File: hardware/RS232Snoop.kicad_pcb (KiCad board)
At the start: 2 copper layers, 29 x 13.2 mm, 11 parts, among them J3 Conn_01x02, J4 Screw_Terminal_01x03, J5 Screw_Terminal_01x03

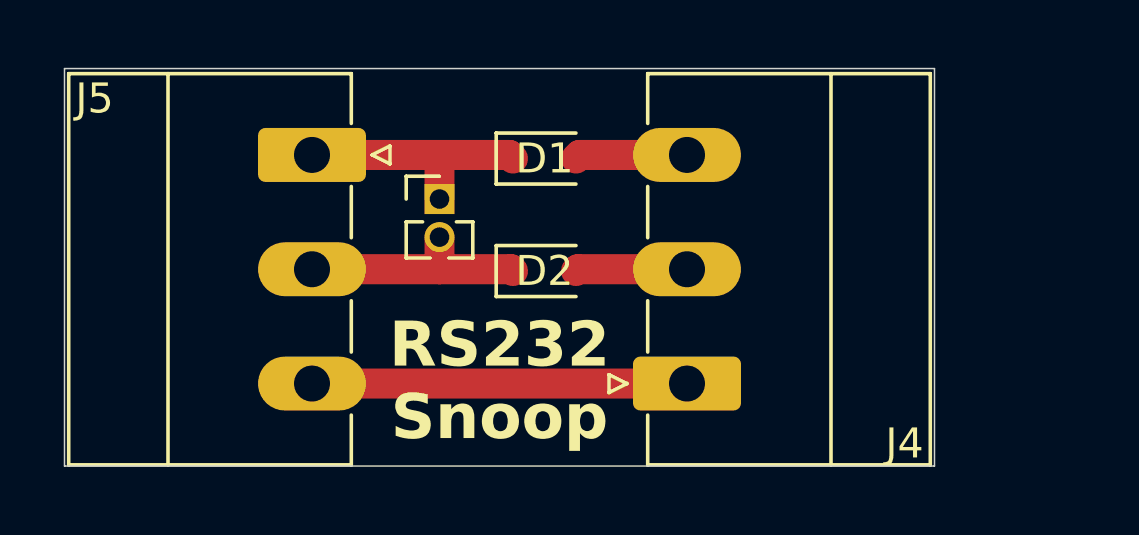
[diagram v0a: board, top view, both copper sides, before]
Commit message: Added headers for straight or crossover
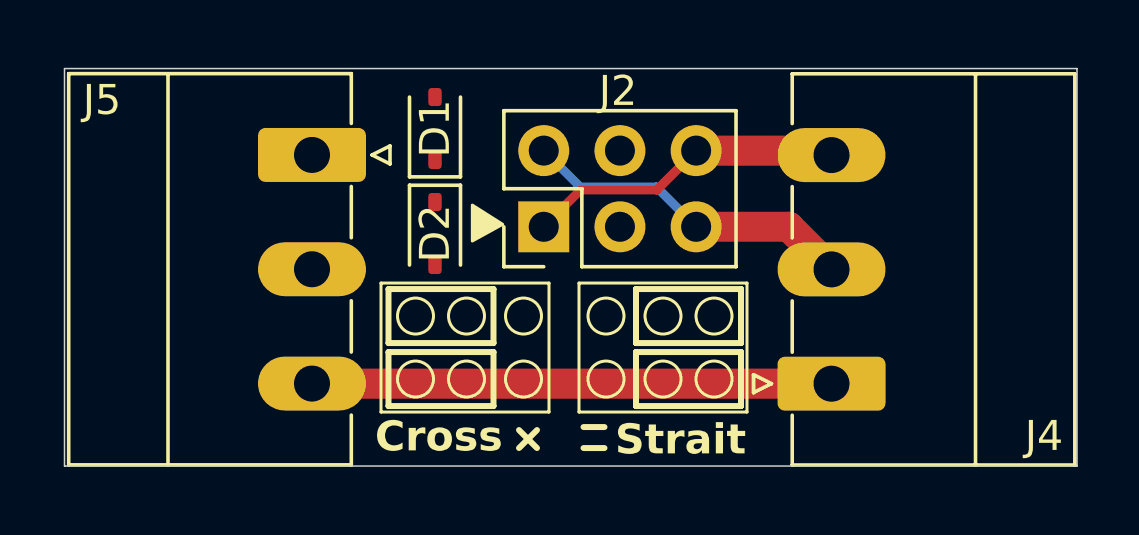
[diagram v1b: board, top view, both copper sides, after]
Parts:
- removed J3: Conn_01x02, Connector_PinHeader_1.27mm:PinHeader_1x02_P1.27mm_Vertical
- added J2: Conn_02x03_Odd_Even, Connector_PinHeader_2.54mm:PinHeader_2x03_P2.54mm_Vertical, F.Cu at (114.7, 56.0)
- moved ? 5.10 mm to (132.4, 50.9)
- moved J4 4.82 mm to (124.3, 61.3)
- moved D2 3.86 mm to (111.1, 56.2), turned to -90 degrees
- moved D1 3.78 mm to (111.1, 52.8), turned to 90 degrees
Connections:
- net Net-(J4-Pin_1) renamed SGND
- D1 pad 2: Net-(D1-A) -> B_TX
- D2 pad 2: Net-(D2-A) -> B_RX
- J4 pad 2: Net-(D2-A) -> A_RX
- J4 pad 3: Net-(D1-A) -> A_TX
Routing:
- net A_RX: track 0.00 -> 11.2 mm
- net A_TX: track 0.00 -> 10.7 mm
- net Net-(D1-K): track 8.22 -> 0.00 mm
- net Net-(D2-K): track 7.79 -> 0.00 mm
- net SGND: track 12.5 -> 17.3 mm
- net Net-(D1-A): track 3.75 -> 0.00 mm
- net Net-(D2-A): track 3.72 -> 0.00 mm
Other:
- board size 29 x 13.2 mm -> 33.8 x 13.2 mm
- board text added: "Chipkin.com 2024/Apr/01"
- board text added: "Cross"
- board text added: "RS232"
- board text added: "SNOOP"
- board text added: "Strait"
- board text removed: "2024/Apr/01"
- board text removed: "Chipkin.com"
- board text removed: "RS232 Snoop"
